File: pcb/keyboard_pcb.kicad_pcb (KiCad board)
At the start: 2 copper layers, 138.8 x 89.9 mm, 23 parts, among them J1 TRRS, K00 KEYSW, K01 KEYSW, K02 KEYSW, K03 KEYSW, K04 KEYSW, K05 KEYSW, K10 KEYSW, K11 KEYSW, K12 KEYSW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

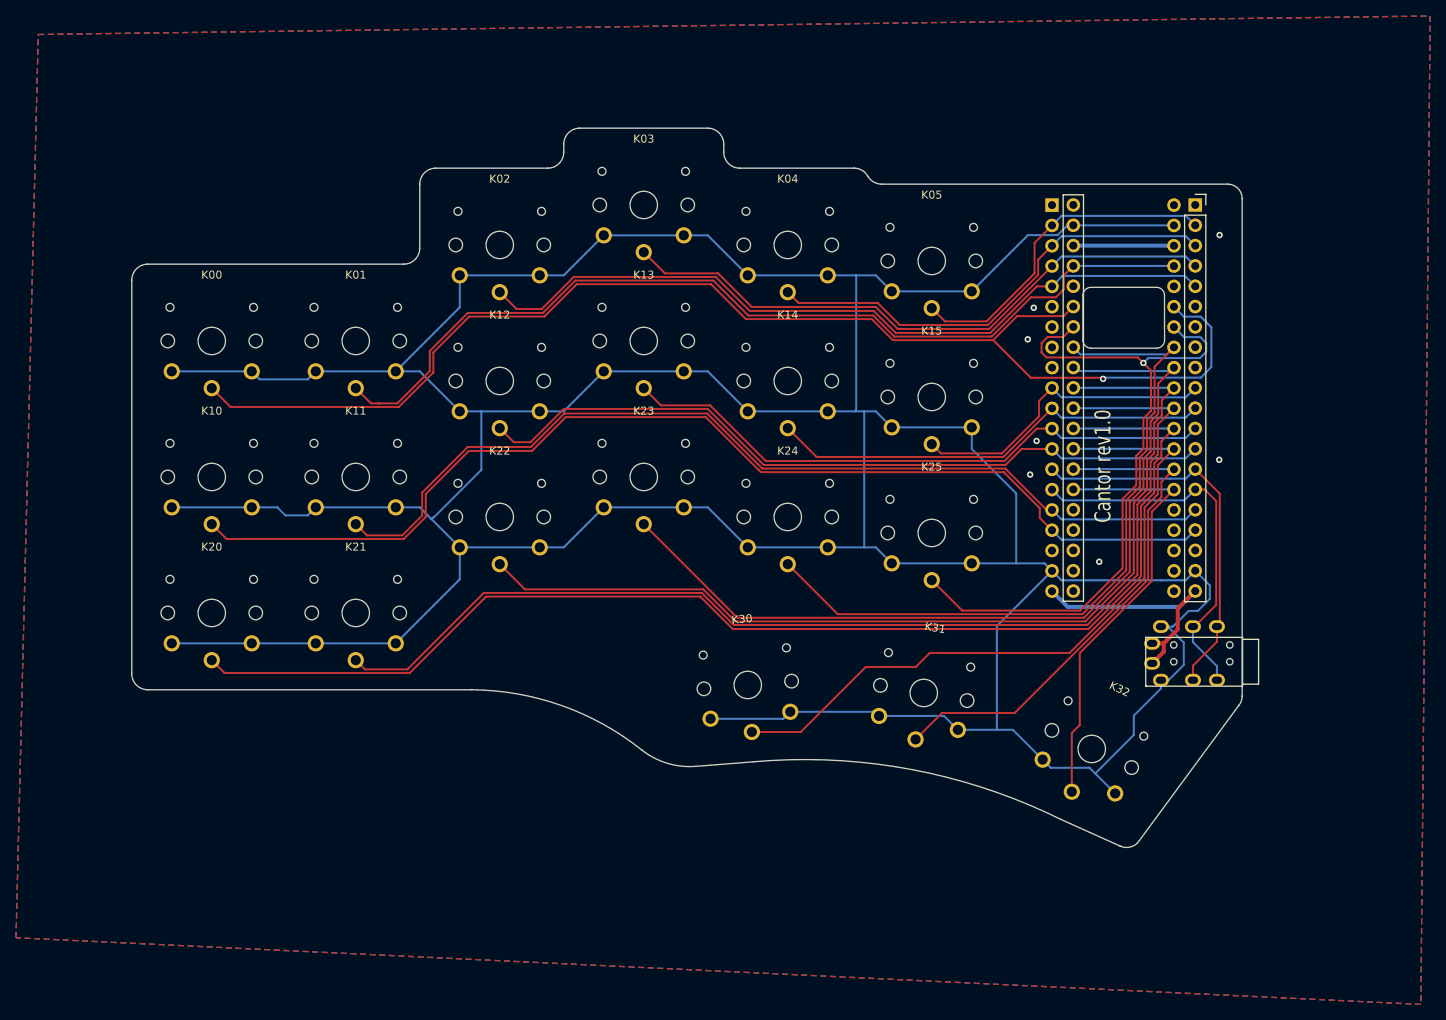
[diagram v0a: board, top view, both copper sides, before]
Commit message: Mod to 36 keys and add silkscreen
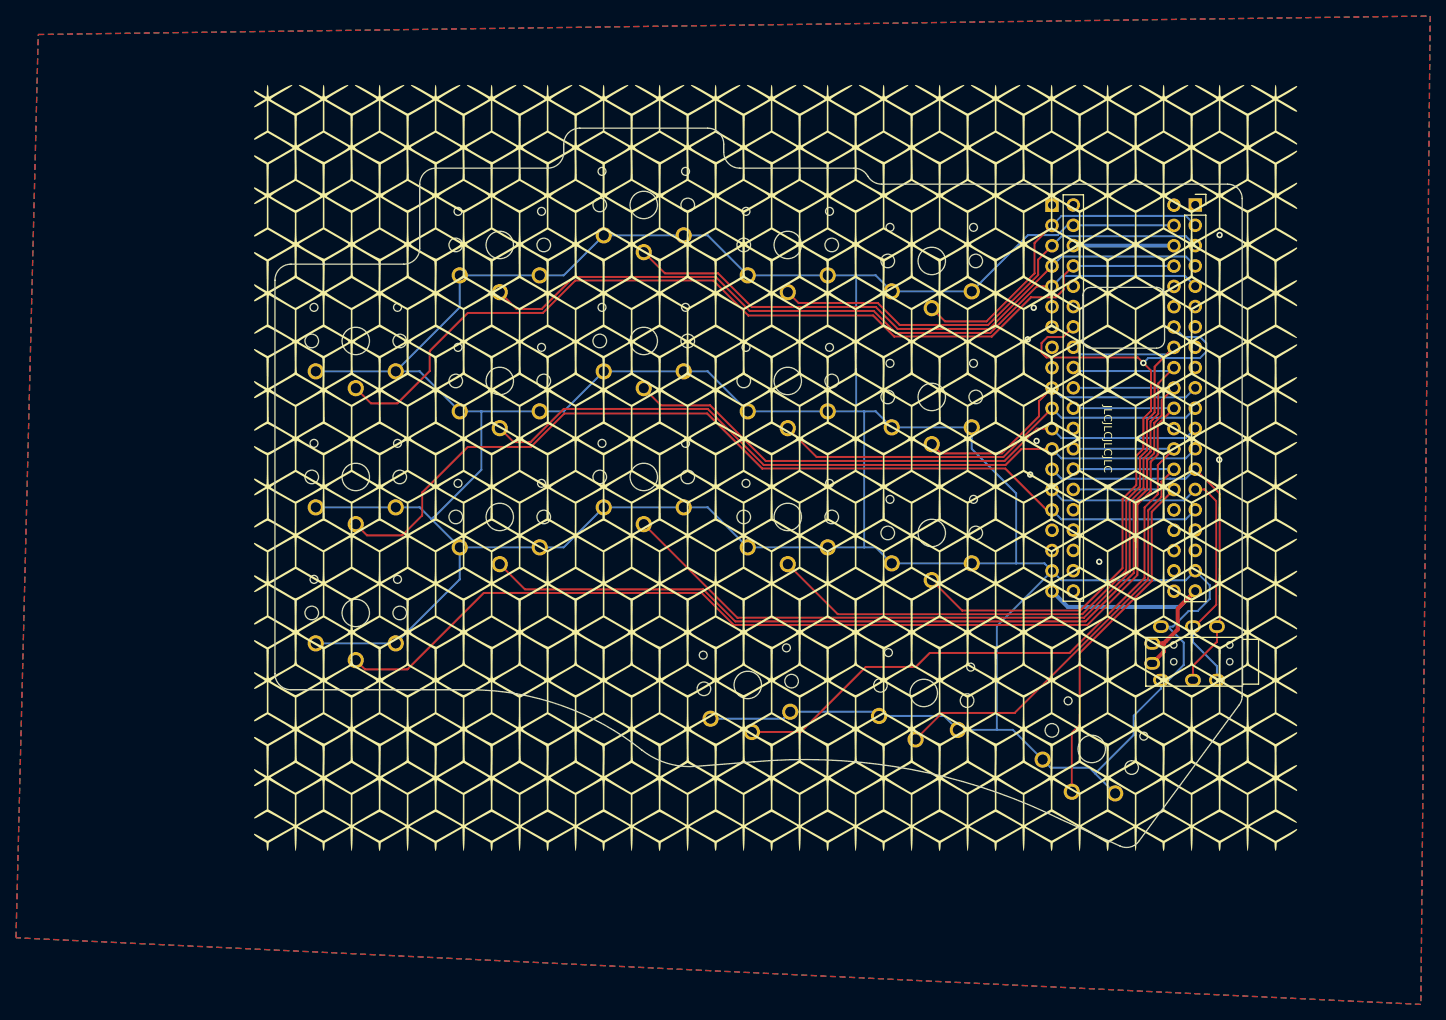
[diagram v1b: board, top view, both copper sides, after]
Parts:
- removed K00, K10, K20: KEYSW, keyswitches:SW_PG1350_reversible
- added G***: LOGO, Footprints:iso_cubes, F.Cu at (144.8, 86.0)
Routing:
- net /k00: track 161.7 -> 0.00 mm, vias 1 -> 0
- net /k20: track 157.9 -> 0.03 mm
- net /k10: track 139.2 -> 0.00 mm
- net GND: track 586.2 -> 530.6 mm
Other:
- board size 138.8 x 89.9 mm -> 120.9 x 89.9 mm
- board text added: "JLCJLCJLCJLC"
- board text removed: "Cantor"
- board text removed: "Cantor rev1.0"
